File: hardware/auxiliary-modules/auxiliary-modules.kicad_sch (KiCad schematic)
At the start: 38 parts, among them J1 IDC-10, J2 Conn_01x07, J3 Conn_01x04, J4 IDC-10, J5 IDC-10, U1 CS49E, U2 NTS0102, U3 LM393, U4 NTS0102

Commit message: Mouser
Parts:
- removed L1, L2, L3, L4, L5: 2.2u/1A, Inductor_SMD:L_0603_1608Metric, symbol Device:L
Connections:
- net FLOW_3.3V: now also C13.1, J5.4 (Pin_4)
- net RANGE_3.3V: now also C10.1, J4.4 (Pin_4)
- net RANGE_5V: now also C7.1, J4.2 (Pin_2)
- net TACH_3.3V: now also C4.1, J1.4 (Pin_4)
- net TACH_5V: now also C1.1, J1.2 (Pin_2)
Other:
- moved on the sheet: C11, C12, C14, C15, C2, C3, C5, C6, C8, C9

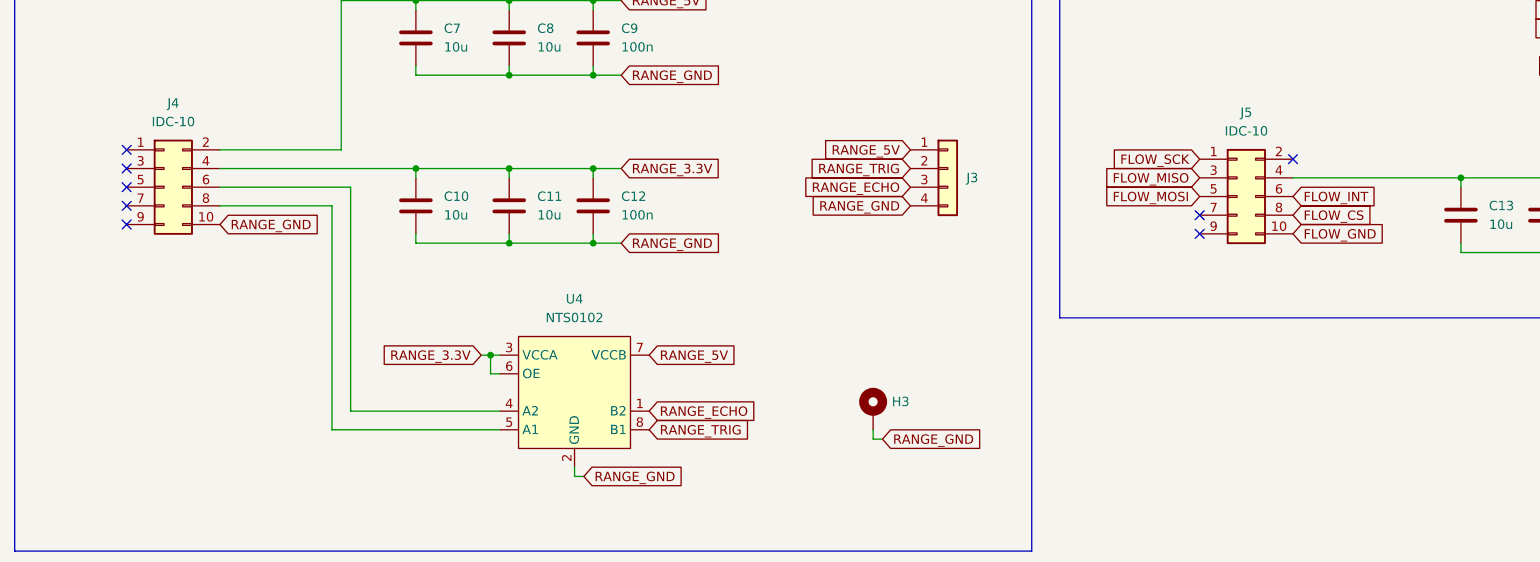
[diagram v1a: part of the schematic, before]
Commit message: fix connector GPS pinout, update AUX pinouts
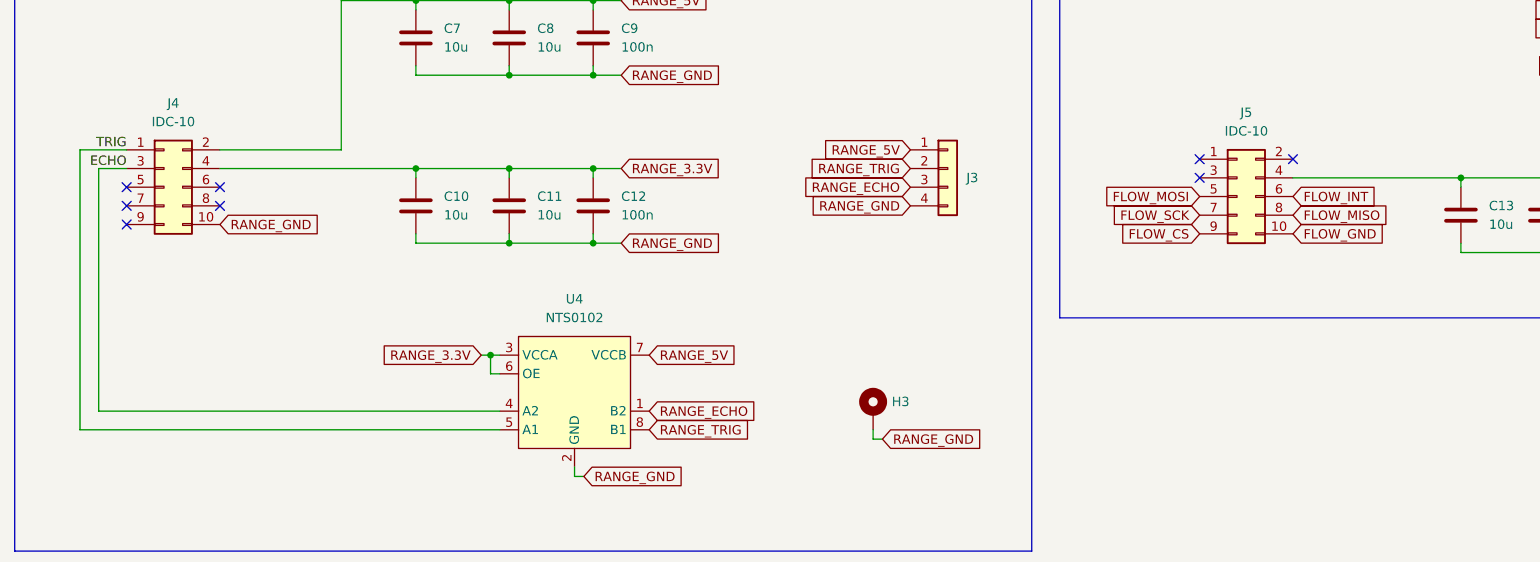
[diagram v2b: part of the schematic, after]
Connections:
- net FLOW_CS: now also J5.9 (Pin_9); no longer J5.8 (Pin_8)
- net FLOW_MISO: now also J5.8 (Pin_8); no longer J5.3 (Pin_3)
- net FLOW_SCK: now also J5.7 (Pin_7); no longer J5.1 (Pin_1)
- net TRIG: now reaches J4.1 (Pin_1)
- net TRIG: now also U4.5 (A1)
- net ECHO: now reaches J4.3 (Pin_3)
- net ECHO: now also U4.4 (A2)
- net at J4.6 (Pin_6): no longer U4.4 (A2)
- net at J4.8 (Pin_8): no longer U4.5 (A1)

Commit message: routing: AUX all
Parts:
- R1, R3, R4, R5: footprint Resistor_SMD:R_0603_1608Metric -> Resistor_SMD:R_0805_2012Metric
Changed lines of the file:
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@@
 			)
 		)
-		(property "Footprint" "Resistor_SMD:R_0603_1608Metric"
+		(property "Footprint" "Resistor_SMD:R_0805_2012Metric"
 			(at 168.91 47.498 90)
 			(effects
@@
 			)
 		)
-		(property "Footprint" "Resistor_SMD:R_0603_1608Metric"
+		(property "Footprint" "Resistor_SMD:R_0805_2012Metric"
 			(at 141.478 45.72 90)
 			(effects
@@
 			)
 		)
-		(property "Footprint" "Resistor_SMD:R_0603_1608Metric"
+		(property "Footprint" "Resistor_SMD:R_0805_2012Metric"
 			(at 141.478 55.88 90)
 			(effects
@@
 			)
 		)
-		(property "Footprint" "Resistor_SMD:R_0603_1608Metric"
+		(property "Footprint" "Resistor_SMD:R_0805_2012Metric"
 			(at 185.42 41.148 90)
 			(effects
